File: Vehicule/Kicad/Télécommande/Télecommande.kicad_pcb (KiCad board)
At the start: 2 copper layers, 77.7 x 40 mm, 5 parts, among them J1 Conn_01x02_Socket, U1 ESP32-C3_SUPERMINI

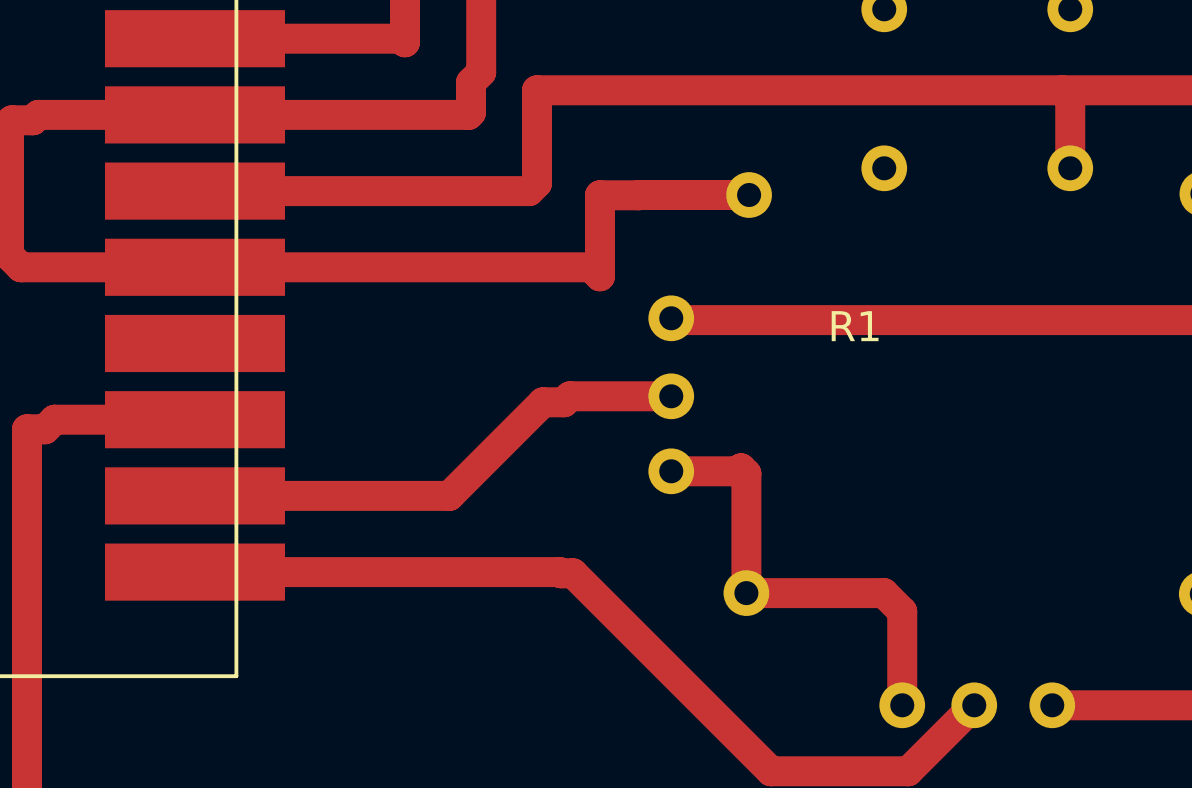
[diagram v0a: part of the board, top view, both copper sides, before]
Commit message: Transfert du SUPERMINI (composant et empreintes) dans les librairies locales (Anumby et Empreintes) Renommer Empreintes -> Anumby
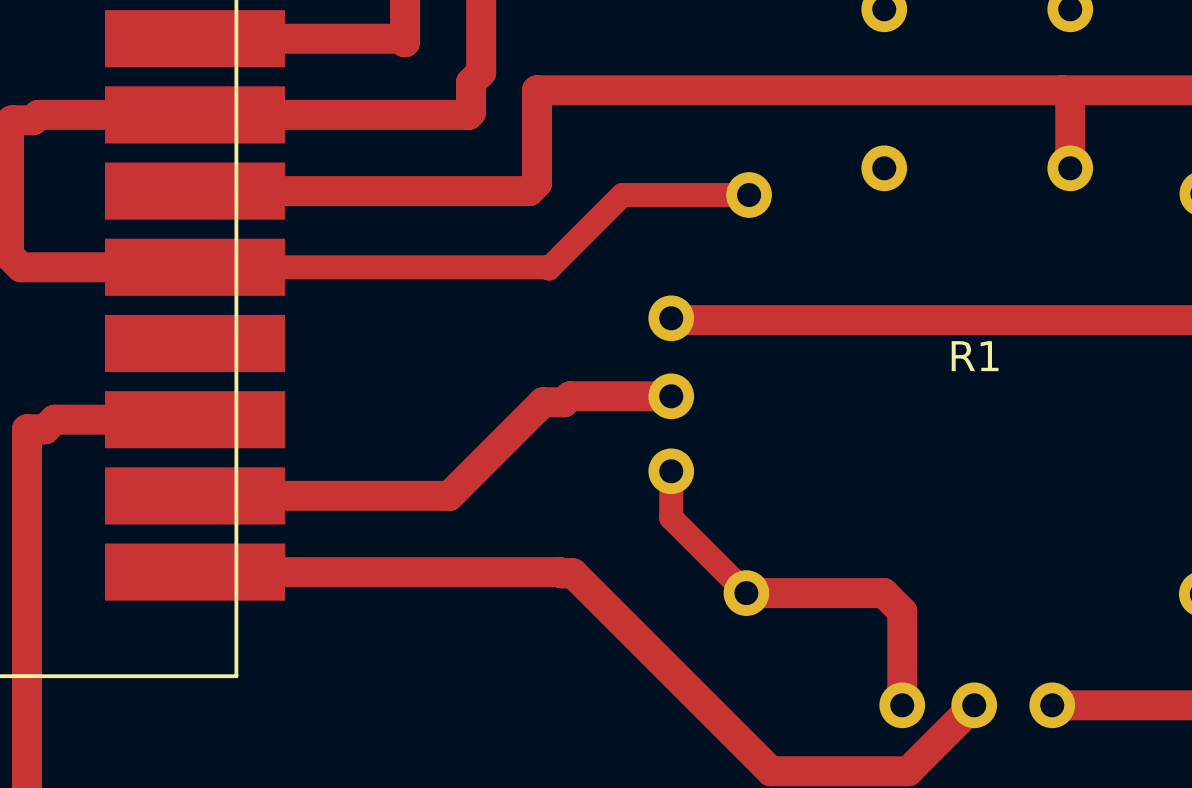
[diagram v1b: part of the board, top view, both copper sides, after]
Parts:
- J1: footprint Empreintes:CONN-2-PINS -> Anumby:CONN-2-PINS
- R1: footprint Empreintes:Joystick -> Anumby:Joystick
- U1: footprint PCM_Espressif:ESP32-C3-SUPERMINI -> Anumby:ESP32-C3-SUPERMINI
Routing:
- net GND: track 72.8 -> 69.5 mm
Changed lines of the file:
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@@
 		)
 	)
-	(footprint "Empreintes:Joystick"
+	(footprint "Anumby:Joystick"
 		(layer "F.Cu")
 		(at 96.1 71.26)
 		(property "Reference" "R1"
-			(at -4 -1 0)
+			(at 0 0 0)
 			(unlocked yes)
 			(layer "F.SilkS")
@@
 			)
 		)
-		(property "Footprint" "Empreintes:Joystick"
+		(property "Footprint" "Anumby:Joystick"
 			(at 1.675 0.3 0)
 			(unlocked yes)
@@
 		)
 	)
-	(footprint "Empreintes:CONN-2-PINS"
+	(footprint "Anumby:CONN-2-PINS"
 		(layer "F.Cu")
 		(at 78.37 53.26)
@@
 			)
 		)
-		(property "Footprint" "Empreintes:CONN-2-PINS"
+		(property "Footprint" "Anumby:CONN-2-PINS"
 			(at 0 0 0)
 			(unlocked yes)
@@
 		)
 	)
-	(footprint "PCM_Espressif:ESP32-C3-SUPERMINI"
+	(footprint "Anumby:ESP32-C3-SUPERMINI"
 		(layer "F.Cu")
 		(at 62.48 70.54)
@@
 			)
 		)
-		(property "Footprint" "PCM_Espressif:ESP32-C3-SUPERMINI"
+		(property "Footprint" "Anumby:ESP32-C3-SUPERMINI"
 			(at 0 0 0)
 			(layer "F.Fab")
@@
 	)
 	(segment
-		(start 84.91 65.85)
-		(end 88.57 65.85)
-		(width 1)
+		(start 88.57 65.85)
+		(end 84.35 65.85)
+		(width 0.8)
 		(layer "F.Cu")
 		(net 23)
@@
 	)
 	(segment
-		(start 88.2 75.06)
-		(end 88.3 74.96)
-		(width 1)
-		(layer "F.Cu")
-		(net 23)
-	)
-	(segment
 		(start 64.7 63.36)
 		(end 64.88 63.18)
@@
 	)
 	(segment
-		(start 88.3 74.96)
-		(end 88.48 75.14)
-		(width 1)
-		(layer "F.Cu")
-		(net 23)
-	)
-	(segment
 		(start 63.9 67.86)
 		(end 63.9 63.46)
@@
 	)
 	(segment
-		(start 70.1 68.26)
-		(end 83.3 68.26)
-		(width 1)
-		(layer "F.Cu")
-		(net 23)
-	)
-	(segment
 		(start 93.06 79.12)
 		(end 93.675 79.735)
@@
 	)
 	(segment
-		(start 88.48 75.14)
-		(end 88.48 79.12)
-		(width 1)
-		(layer "F.Cu")
-		(net 23)
-	)
-	(segment
-		(start 83.6 68.56)
-		(end 83.6 65.86)
-		(width 1)
-		(layer "F.Cu")
-		(net 23)
-	)
-	(segment
 		(start 79.3 63.1)
 		(end 79.3 62.1)
@@
 	)
 	(segment
-		(start 84.9 65.86)
-		(end 84.91 65.85)
-		(width 1)
-		(layer "F.Cu")
-		(net 23)
-	)
-	(segment
-		(start 83.6 65.86)
-		(end 84.9 65.86)
-		(width 1)
+		(start 85.975 76.615)
+		(end 88.48 79.12)
+		(width 0.8)
+		(layer "F.Cu")
+		(net 23)
+	)
+	(segment
+		(start 85.975 75.06)
+		(end 85.975 76.615)
+		(width 0.8)
+		(layer "F.Cu")
+		(net 23)
+	)
+	(segment
+		(start 81.86 68.26)
+		(end 70.1 68.26)
+		(width 0.8)
 		(layer "F.Cu")
 		(net 23)
@@
 	)
 	(segment
-		(start 85.975 75.06)
-		(end 88.2 75.06)
-		(width 1)
-		(layer "F.Cu")
-		(net 23)
-	)
-	(segment
-		(start 83.3 68.26)
-		(end 83.6 68.56)
-		(width 1)
-		(layer "F.Cu")
-		(net 23)
+		(start 81.9 68.3)
+		(end 81.86 68.26)
+		(width 0.8)
+		(layer "F.Cu")
+		(net 23)
+	)
+	(segment
+		(start 84.35 65.85)
+		(end 81.9 68.3)
+		(width 0.8)
+		(layer "F.Cu")
+		(net 23)

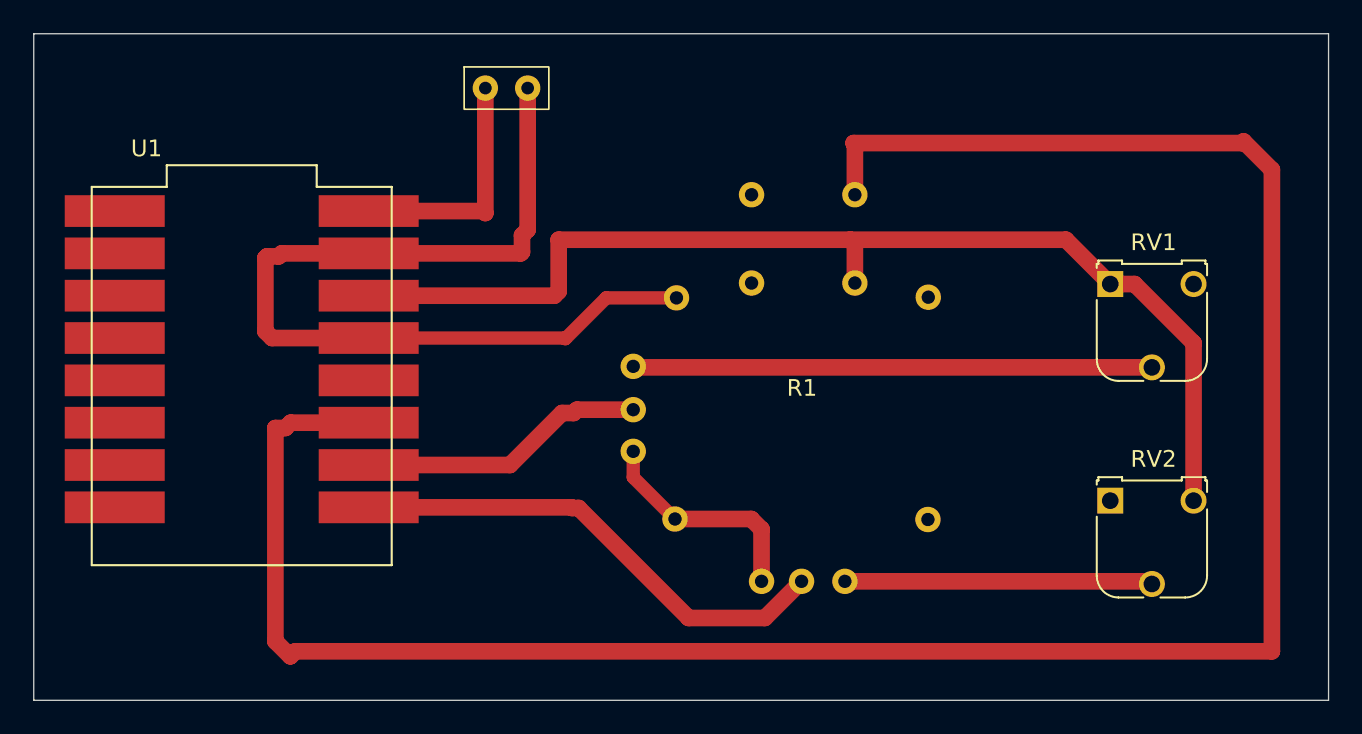
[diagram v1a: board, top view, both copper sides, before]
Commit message: TAjouter la couche de masse pour la télécommande
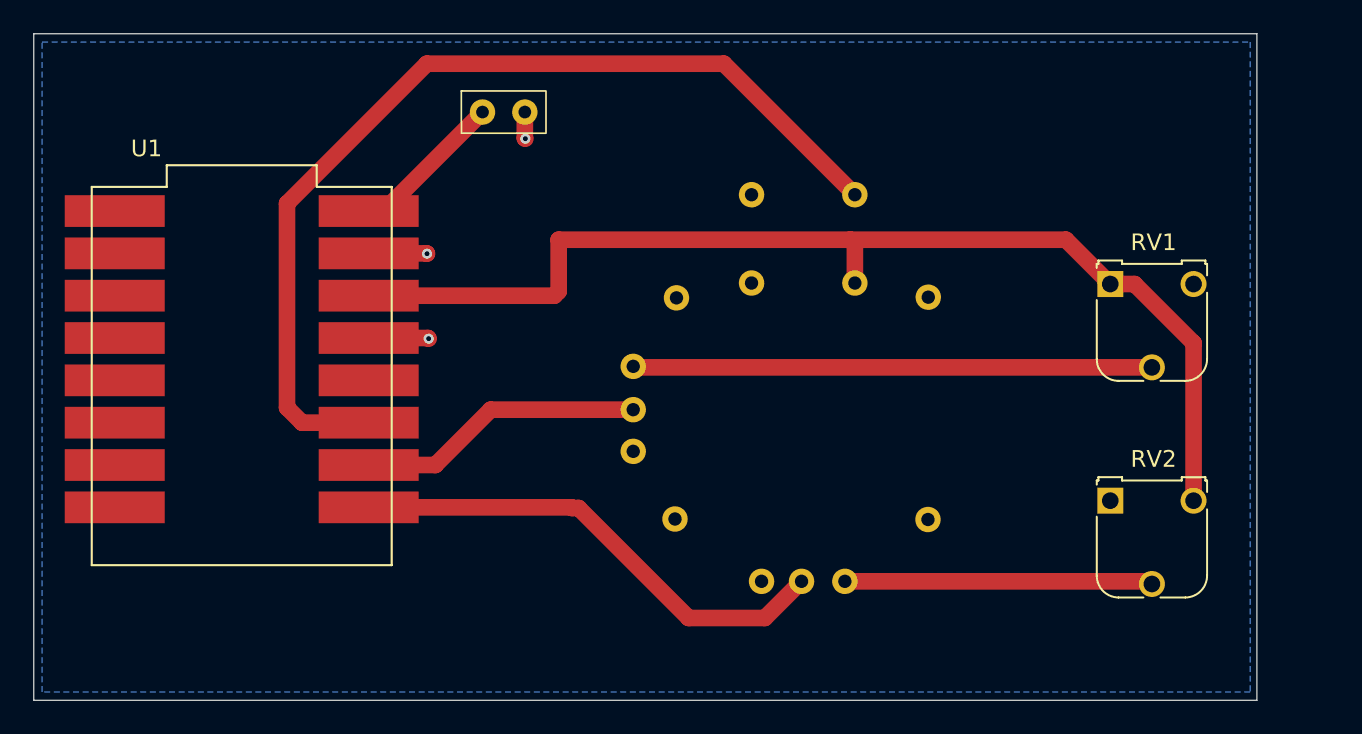
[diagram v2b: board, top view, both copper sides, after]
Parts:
- moved J1 1.45 mm to (78.2, 54.7)
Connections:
- net Net-(R1-H) renamed /H
- net Net-(R1-H+-Pad6) renamed /H+
- net Net-(R1-V) renamed /V
- net Net-(R1-V+) renamed /V+
- net Net-(U1-GPIO2) renamed /B2
- R1 pad 12: unconnected-(R1-MP-Pad12) -> GND
- R1 pad 13: unconnected-(R1-MP-Pad13) -> GND
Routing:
- net /B2: track 136.7 -> 58.3 mm
- net GND: track 69.5 -> 8.74 mm, vias 0 -> 3
- net 5V: track 14.5 -> 9.29 mm
- added copper zone on B.Cu, net GND
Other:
- board size 77.7 x 40 mm -> 73.4 x 40 mm

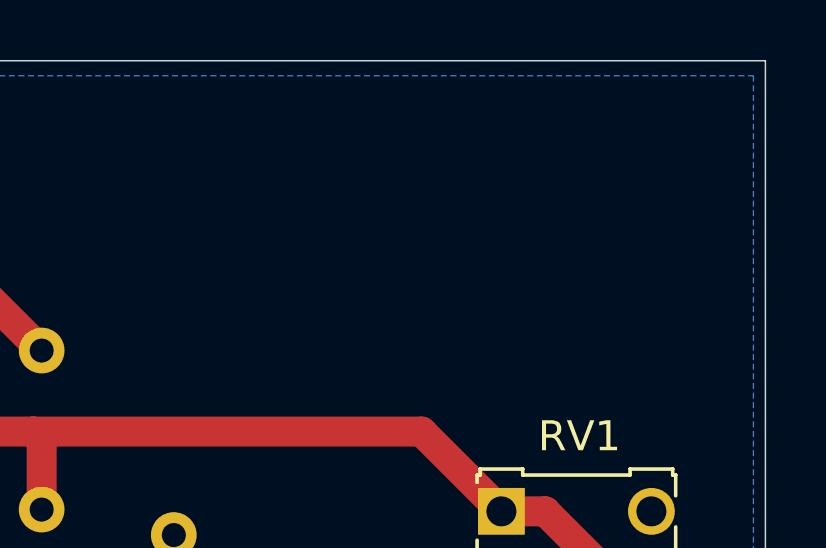
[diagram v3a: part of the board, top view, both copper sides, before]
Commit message: Ajout de logo Anumby pour PCB (2 versions)
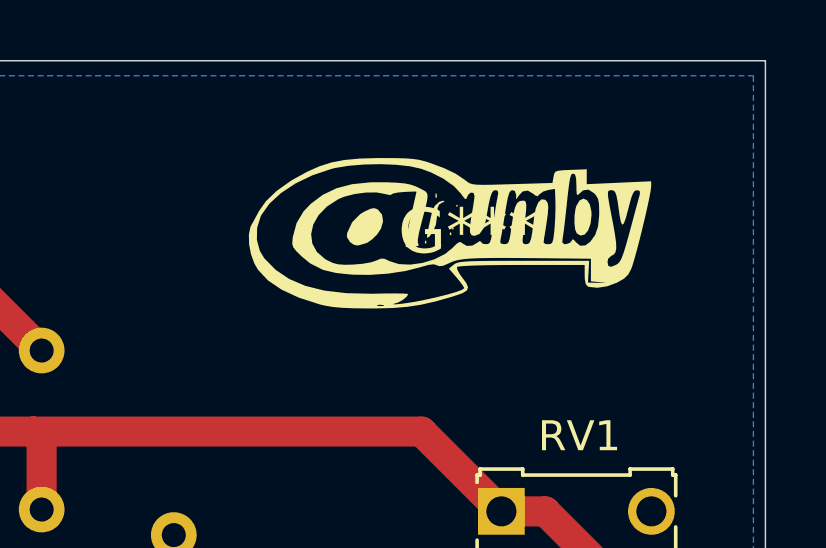
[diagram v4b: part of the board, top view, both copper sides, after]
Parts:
- added G***: LOGO, Anumby:Logo_Anumby_15, F.Cu at (113.5, 55.7)

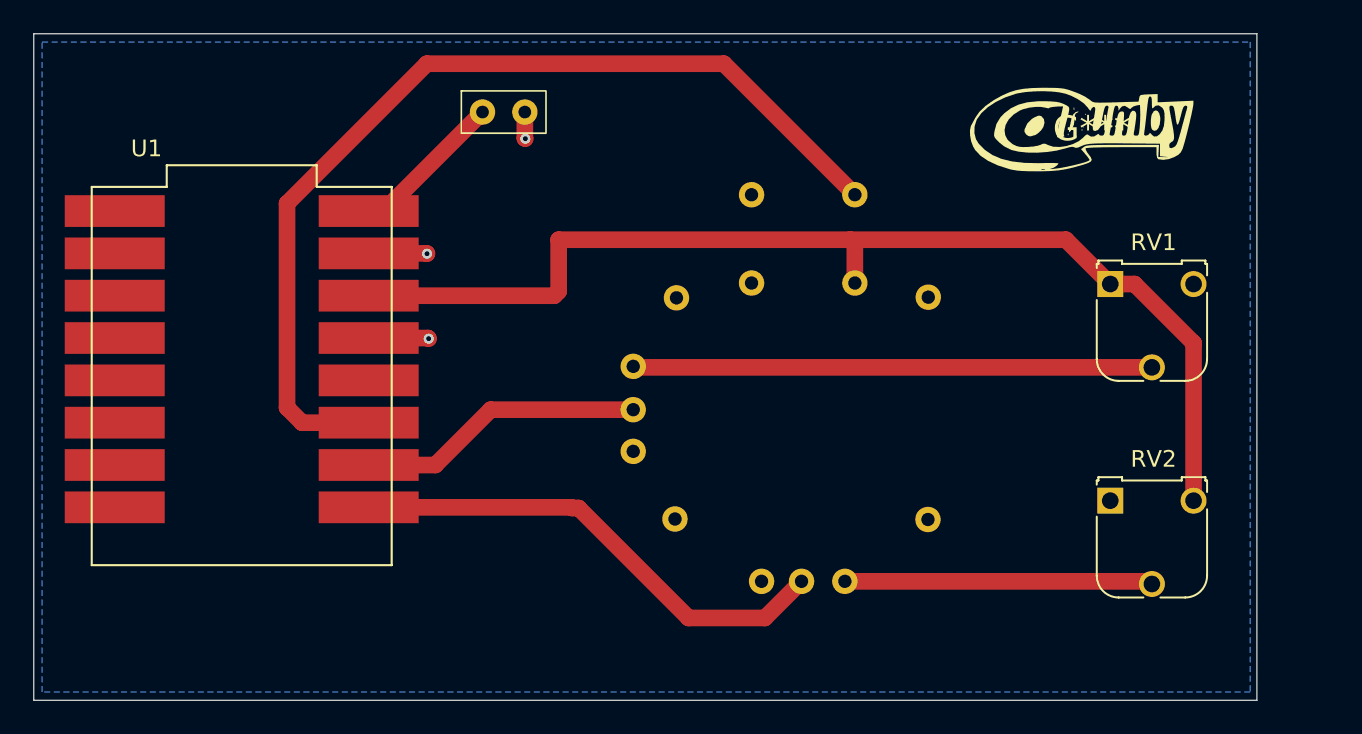
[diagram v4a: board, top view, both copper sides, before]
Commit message: Ajout de logo Anumby pour PCB Mise à jour des empreintes, des connecteurs des librairies
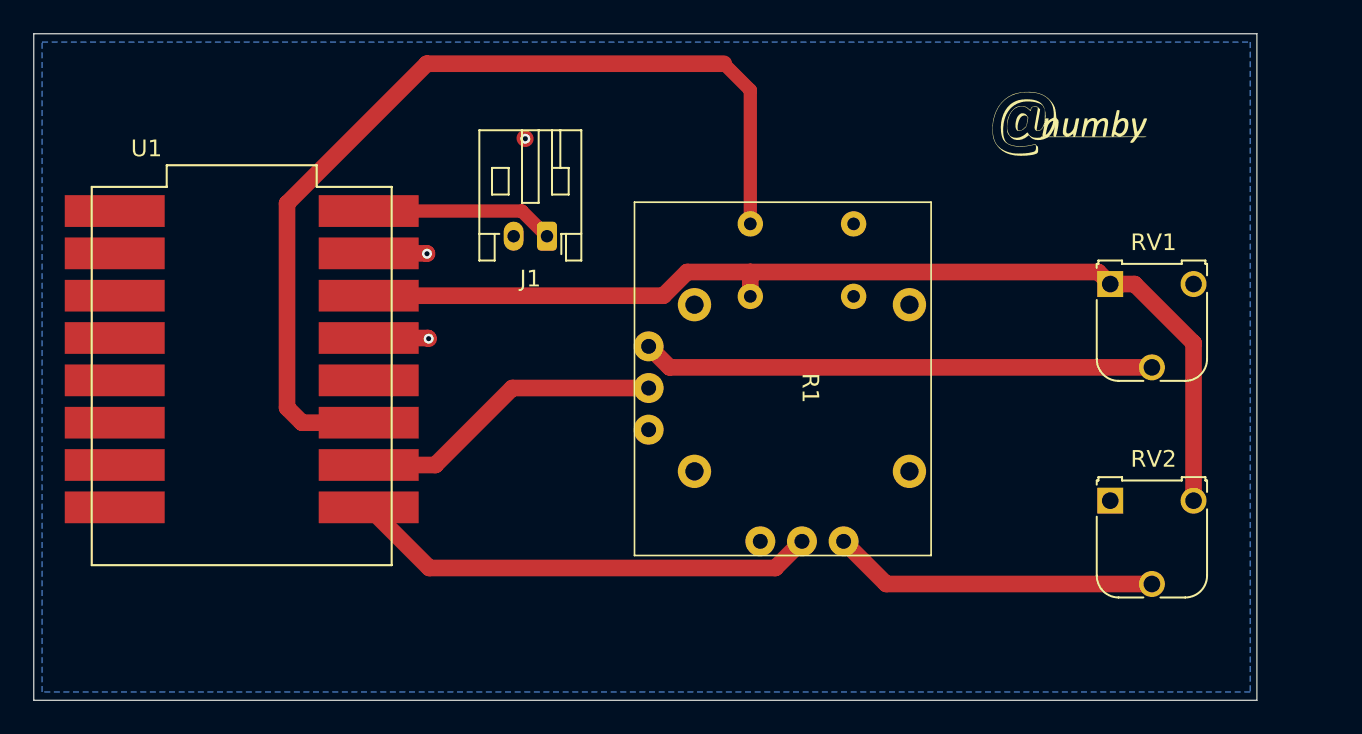
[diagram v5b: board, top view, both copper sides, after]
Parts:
- removed G***: LOGO, Anumby:Logo_Anumby_15
- added G: Val**, Anumby:Logo_Anumby_10, F.Cu at (112.2, 55.4)
- J1: footprint Anumby:CONN-2-PINS -> Connector_JST:JST_PH_S2B-PH-K_1x02_P2.00mm_Horizontal
- R1: footprint Anumby:Joystick -> Anumby:JOYSTICK_MODEL_802
- moved J1 7.89 mm to (80.8, 62.1), turned to 180 degrees
- turned R1 to -90 degrees
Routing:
- net 3V3: track 67.4 -> 62.8 mm
- net 5V: track 9.29 -> 12.3 mm, vias 0 -> 1
- net GND: track 8.74 -> 7.12 mm, vias 3 -> 2
- net /H: track 29.6 -> 28.2 mm
- net /V: track 17.3 -> 18.7 mm
- net /H+: track 18.5 -> 19.8 mm
- net /B2: track 58.3 -> 57.5 mm
